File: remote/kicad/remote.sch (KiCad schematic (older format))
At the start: 20 parts, among them J1 USB_B_Micro, U1 stm32, U2 cc2500, U3 LCD1602_I2c, U4 LI_Charger

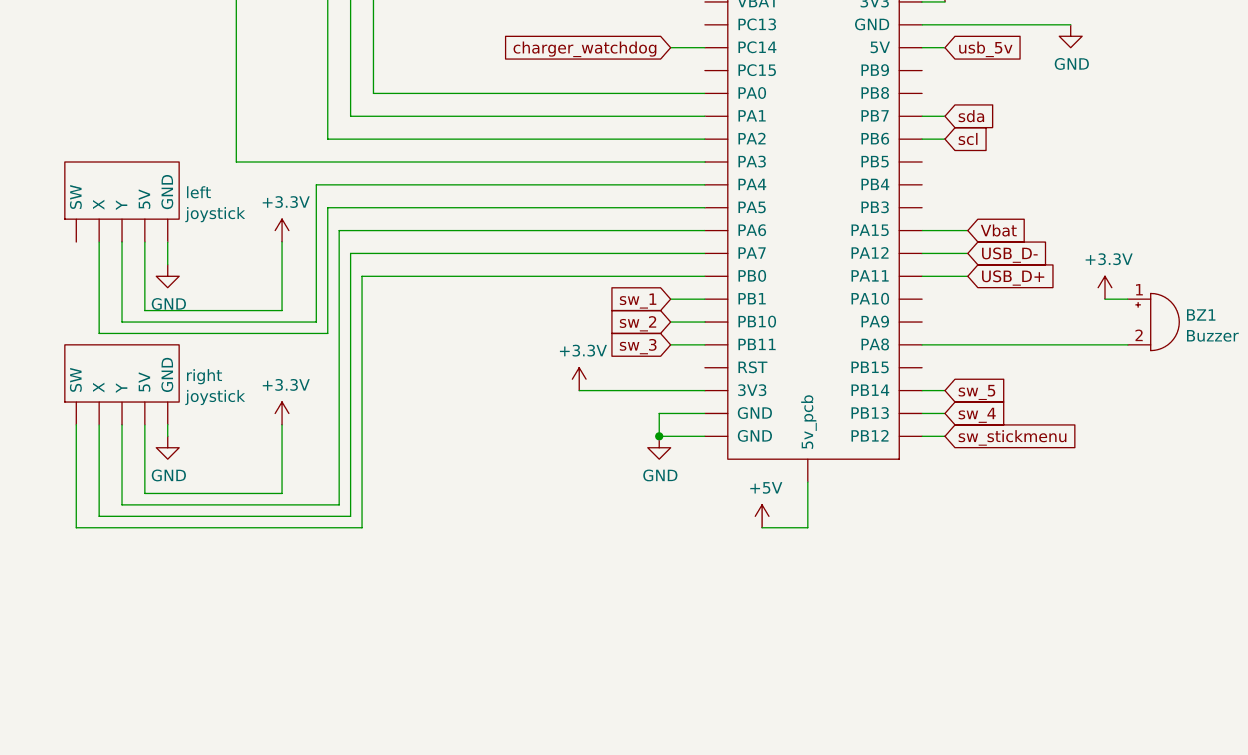
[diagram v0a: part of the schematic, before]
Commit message: change vbat to a analog pin
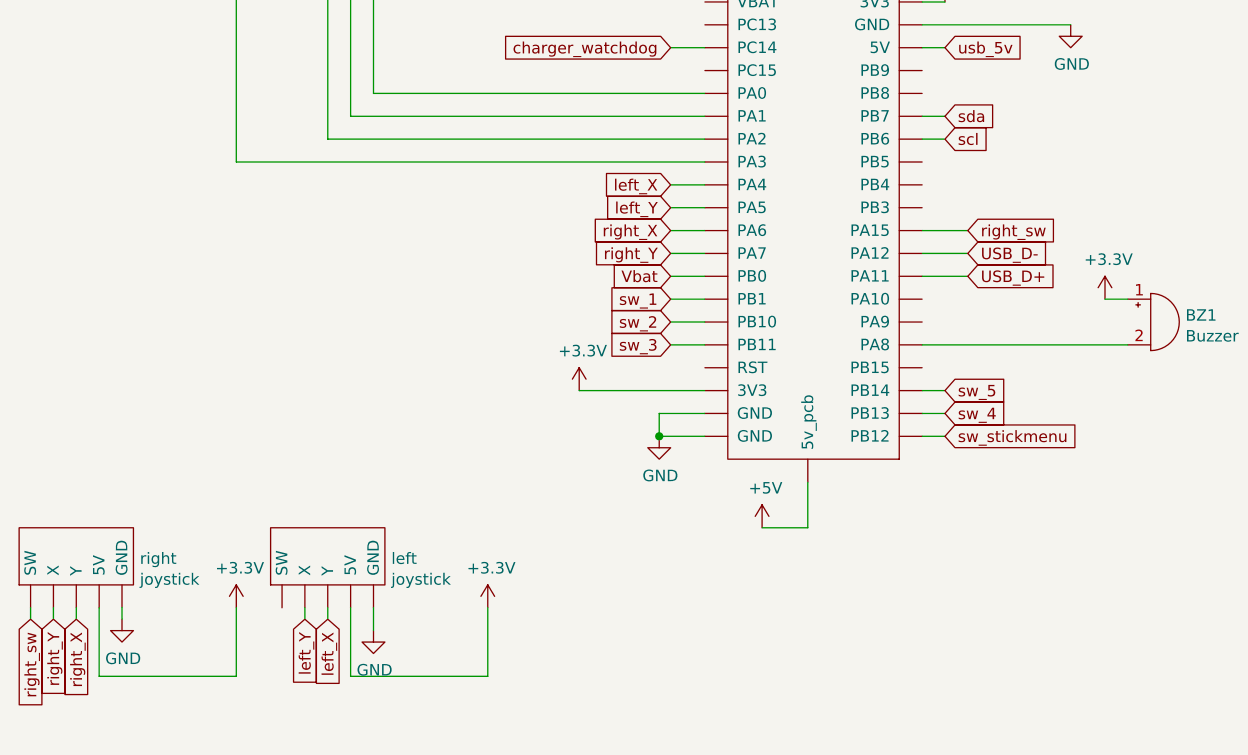
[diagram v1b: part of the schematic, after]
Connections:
- net left_Y: now reaches U1.~ (VBAT), left.~ (Y)
- net right_sw: now reaches U1.~ (VBAT), right.~ (Y)
- new net: U1.~ (VBAT), U2.~ (VCC) (x4)
- new net left_X: U1.~ (VBAT), left.~ (Y)
- new net right_X: U1.~ (VBAT), right.~ (Y)
- new net right_Y: U1.~ (VBAT), right.~ (Y)
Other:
- moved on the sheet: left, right
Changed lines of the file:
@@
 L remote-rescue:joystick-remote left
 U 1 1 5C49DC62
-P 1400 5000
-F 0 "left" H 1978 5365 50  0000 L CNN
-F 1 "joystick" H 1978 5274 50  0000 L CNN
-F 2 "" H 1900 5550 50  0001 C CNN
-F 3 "" H 1900 5550 50  0001 C CNN
-	1    1400 5000
-	1    0    0    -1
-$EndComp
-$Comp
-L remote-rescue:joystick-remote right
-U 1 1 5C49FFCD
-P 1400 5800
-F 0 "right" H 1978 6165 50  0000 L CNN
-F 1 "joystick" H 1978 6074 50  0000 L CNN
-F 2 "" H 1900 6350 50  0001 C CNN
-F 3 "" H 1900 6350 50  0001 C CNN
-	1    1400 5800
-	1    0    0    -1
-$EndComp
-Wire Wire Line
-	1900 4850 1900 4950
-Wire Wire Line
-	1700 4850 1700 5200
-Wire Wire Line
-	1600 5250 1600 4850
-Wire Wire Line
-	1700 5650 1700 6000
-Wire Wire Line
-	1600 6050 1600 5650
+P 2300 6600
+F 0 "left" H 2878 6965 50  0000 L CNN
+F 1 "joystick" H 2878 6874 50  0000 L CNN
+F 2 "" H 2800 7150 50  0001 C CNN
+F 3 "" H 2800 7150 50  0001 C CNN
+	1    2300 6600
+	1    0    0    -1
+$EndComp
+Wire Wire Line
+	2800 6450 2800 6550
 $Comp
 L power:+3.3V #PWR?
@@
 L power:+3.3V #PWR?
 U 1 1 5C539EAE
-P 2400 4850
-F 0 "#PWR?" H 2400 4700 50  0001 C CNN
-F 1 "+3.3V" H 2415 5023 50  0000 C CNN
-F 2 "" H 2400 4850 50  0001 C CNN
-F 3 "" H 2400 4850 50  0001 C CNN
-	1    2400 4850
+P 3300 6450
+F 0 "#PWR?" H 3300 6300 50  0001 C CNN
+F 1 "+3.3V" H 3315 6623 50  0000 C CNN
+F 2 "" H 3300 6450 50  0001 C CNN
+F 3 "" H 3300 6450 50  0001 C CNN
+	1    3300 6450
 	1    0    0    -1
 $EndComp
@@
 L power:+3.3V #PWR?
 U 1 1 5C539EFA
-P 2400 5650
-F 0 "#PWR?" H 2400 5500 50  0001 C CNN
-F 1 "+3.3V" H 2415 5823 50  0000 C CNN
-F 2 "" H 2400 5650 50  0001 C CNN
-F 3 "" H 2400 5650 50  0001 C CNN
-	1    2400 5650
+P 2200 6450
+F 0 "#PWR?" H 2200 6300 50  0001 C CNN
+F 1 "+3.3V" H 2215 6623 50  0000 C CNN
+F 2 "" H 2200 6450 50  0001 C CNN
+F 3 "" H 2200 6450 50  0001 C CNN
+	1    2200 6450
 	1    0    0    -1
 $EndComp
@@
 L power:GND #PWR?
 U 1 1 5C56BD86
-P 1900 5700
-F 0 "#PWR?" H 1900 5450 50  0001 C CNN
-F 1 "GND" H 1905 5527 50  0000 C CNN
-F 2 "" H 1900 5700 50  0001 C CNN
-F 3 "" H 1900 5700 50  0001 C CNN
-	1    1900 5700
-	1    0    0    -1
-$EndComp
-Wire Wire Line
-	1900 5650 1900 5700
-Wire Wire Line
-	1800 5650 1800 5950
-Wire Wire Line
-	1800 5950 2400 5950
-Wire Wire Line
-	2400 5950 2400 5650
+P 1700 6500
+F 0 "#PWR?" H 1700 6250 50  0001 C CNN
+F 1 "GND" H 1705 6327 50  0000 C CNN
+F 2 "" H 1700 6500 50  0001 C CNN
+F 3 "" H 1700 6500 50  0001 C CNN
+	1    1700 6500
+	1    0    0    -1
+$EndComp
+Wire Wire Line
+	1700 6450 1700 6500
+Wire Wire Line
+	1600 6450 1600 6750
+Wire Wire Line
+	1600 6750 2200 6750
+Wire Wire Line
+	2200 6750 2200 6450
 $Comp
 L power:GND #PWR?
 U 1 1 5C585C56
-P 1900 4950
-F 0 "#PWR?" H 1900 4700 50  0001 C CNN
-F 1 "GND" H 1905 4777 50  0000 C CNN
-F 2 "" H 1900 4950 50  0001 C CNN
-F 3 "" H 1900 4950 50  0001 C CNN
-	1    1900 4950
-	1    0    0    -1
-$EndComp
-Wire Wire Line
-	1800 5150 2400 5150
-Wire Wire Line
-	2400 5150 2400 4850
-Wire Wire Line
-	1800 4850 1800 5150
+P 2800 6550
+F 0 "#PWR?" H 2800 6300 50  0001 C CNN
+F 1 "GND" H 2805 6377 50  0000 C CNN
+F 2 "" H 2800 6550 50  0001 C CNN
+F 3 "" H 2800 6550 50  0001 C CNN
+	1    2800 6550
+	1    0    0    -1
+$EndComp
+Wire Wire Line
+	2700 6750 3300 6750
+Wire Wire Line
+	3300 6750 3300 6450
+Wire Wire Line
+	2700 6450 2700 6750
 $Comp
 L power:GND #PWR?
@@
 Wire Wire Line
 	5200 3800 5300 3800
-Wire Wire Line
-	1500 5650 1500 6100
 $Comp
 L Device:R R1
@@
 Wire Wire Line
 	5850 1700 5900 1700
-Wire Wire Line
-	2550 4600 2550 5200
-Wire Wire Line
-	2550 5200 1700 5200
-Wire Wire Line
-	2550 4600 4250 4600
-Wire Wire Line
-	2600 4700 2600 5250
-Wire Wire Line
-	2600 5250 1600 5250
-Wire Wire Line
-	2600 4700 4250 4700
-Wire Wire Line
-	1700 6000 2650 6000
-Wire Wire Line
-	2650 6000 2650 4800
-Wire Wire Line
-	2650 4800 4250 4800
-Wire Wire Line
-	4250 4900 2700 4900
-Wire Wire Line
-	2700 4900 2700 6050
-Wire Wire Line
-	2700 6050 1600 6050
-Wire Wire Line
-	1500 6100 2750 6100
-Wire Wire Line
-	2750 6100 2750 5000
-Wire Wire Line
-	2750 5000 4250 5000
 Text GLabel 4100 5100 0    50   Input ~ 0
 sw_1
@@
 	10300 2250 10050 2250
 Connection ~ 10050 2250
-Text GLabel 5400 4800 2    50   Input ~ 0
+Text GLabel 4100 5000 0    50   Input ~ 0
 Vbat
 Wire Wire Line
-	5400 4800 5200 4800
+	4100 5000 4250 5000
 Wire Wire Line
 	8800 1250 8800 1650
@@
 Wire Wire Line
 	4250 4000 4100 4000
+Text GLabel 4100 4600 0    50   Input ~ 0
+left_X
+Wire Wire Line
+	4250 4600 4100 4600
+Wire Wire Line
+	2600 6450 2600 6500
+Text GLabel 4100 4700 0    50   Input ~ 0
+left_Y
+Wire Wire Line
+	4250 4700 4100 4700
+Text GLabel 2600 6500 3    50   Input ~ 0
+left_X
+$Comp
+L remote-rescue:joystick-remote right
+U 1 1 5C49FFCD
+P 1200 6600
+F 0 "right" H 1778 6965 50  0000 L CNN
+F 1 "joystick" H 1778 6874 50  0000 L CNN
+F 2 "" H 1700 7150 50  0001 C CNN
+F 3 "" H 1700 7150 50  0001 C CNN
+	1    1200 6600
+	1    0    0    -1
+$EndComp
+Text GLabel 2500 6500 3    50   Input ~ 0
+left_Y
+Wire Wire Line
+	2500 6500 2500 6450
+Text GLabel 4100 4800 0    50   Input ~ 0
+right_X
+Wire Wire Line
+	4250 4800 4100 4800
+Text GLabel 4100 4900 0    50   Input ~ 0
+right_Y
+Wire Wire Line
+	4250 4900 4100 4900
+Wire Wire Line
+	1500 6450 1500 6500
+Wire Wire Line
+	1400 6500 1400 6450
+Wire Wire Line
+	5200 4800 5400 4800
+Text GLabel 5400 4800 2    50   Input ~ 0
+right_sw
+Text GLabel 1400 6500 3    50   Input ~ 0
+right_Y
+Text GLabel 1500 6500 3    50   Input ~ 0
+right_X
+Text GLabel 1300 6500 3    50   Input ~ 0
+right_sw
+Wire Wire Line
+	1300 6450 1300 6500
 $EndSCHEMATC
